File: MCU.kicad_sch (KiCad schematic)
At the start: 1 part, among them U2 STM32L476RGTx

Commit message: Partie écran
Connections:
- net EPD_RST: now reaches U2.15 (PA1)
- net EPD_DC: now reaches U2.16 (PA2)
- net EPD_BUSY: now reaches U2.17 (PA3)
- net EPD_CS: now reaches U2.20 (PA4)
- net EPD_SCK: now reaches U2.21 (PA5)
- net EPD_PWR: now reaches U2.22 (PA6)
- net EPD_DIN: now reaches U2.23 (PA7)
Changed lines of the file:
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@@
 	(wire
 		(pts
-			(xy 113.03 72.39) (xy 125.73 72.39)
+			(xy 114.3 128.27) (xy 125.73 128.27)
+		)
+		(stroke
+			(width 0)
+			(type default)
+		)
+	)
+	(wire
+		(pts
+			(xy 114.3 123.19) (xy 125.73 123.19)
+		)
+		(stroke
+			(width 0)
+			(type default)
+		)
+	)
+	(wire
+		(pts
+			(xy 114.3 72.39) (xy 125.73 72.39)
+		)
+		(stroke
+			(width 0)
+			(type default)
+		)
+	)
+	(wire
+		(pts
+			(xy 114.3 133.35) (xy 125.73 133.35)
 		)
 		(stroke
@@
 	(wire
 		(pts
-			(xy 113.03 69.85) (xy 125.73 69.85)
+			(xy 114.3 118.11) (xy 125.73 118.11)
+		)
+		(stroke
+			(width 0)
+			(type default)
+		)
+	)
+	(wire
+		(pts
+			(xy 114.3 130.81) (xy 125.73 130.81)
+		)
+		(stroke
+			(width 0)
+			(type default)
+		)
+	)
+	(wire
+		(pts
+			(xy 114.3 125.73) (xy 125.73 125.73)
+		)
+		(stroke
+			(width 0)
+			(type default)
+		)
+	)
+	(wire
+		(pts
+			(xy 114.3 69.85) (xy 125.73 69.85)
 		)
 		(stroke
@@
 		)
 	)
+	(wire
+		(pts
+			(xy 114.3 120.65) (xy 125.73 120.65)
+		)
+		(stroke
+			(width 0)
+			(type default)
+		)
+	)
+	(global_label "EPD_BUSY"
+		(shape input)
+		(at 114.3 128.27 180)
+		(fields_autoplaced yes)
+		(effects
+			(font
+				(size 1.27 1.27)
+			)
+			(justify right)
+		)
+		(property "Intersheetrefs" "${INTERSHEET_REFS}"
+			(at 101.7596 128.27 0)
+			(effects
+				(font
+					(size 1.27 1.27)
+				)
+				(justify right)
+				(hide yes)
+			)
+		)
+	)
+	(global_label "EPD_DC"
+		(shape input)
+		(at 114.3 130.81 180)
+		(fields_autoplaced yes)
+		(effects
+			(font
+				(size 1.27 1.27)
+			)
+			(justify right)
+		)
+		(property "Intersheetrefs" "${INTERSHEET_REFS}"
+			(at 104.1182 130.81 0)
+			(effects
+				(font
+					(size 1.27 1.27)
+				)
+				(justify right)
+				(hide yes)
+			)
+		)
+	)
+	(global_label "EPD_CS"
+		(shape input)
+		(at 114.3 125.73 180)
+		(fields_autoplaced yes)
+		(effects
+			(font
+				(size 1.27 1.27)
+			)
+			(justify right)
+		)
+		(property "Intersheetrefs" "${INTERSHEET_REFS}"
+			(at 104.1787 125.73 0)
+			(effects
+				(font
+					(size 1.27 1.27)
+				)
+				(justify right)
+				(hide yes)
+			)
+		)
+	)
 	(global_label "SCL"
 		(shape input)
-		(at 113.03 72.39 180)
-		(fields_autoplaced yes)
-		(effects
-			(font
-				(size 1.27 1.27)
-			)
-			(justify right)
-		)
-		(property "Intersheetrefs" "${INTERSHEET_REFS}"
-			(at 106.5372 72.39 0)
+		(at 114.3 72.39 180)
+		(fields_autoplaced yes)
+		(effects
+			(font
+				(size 1.27 1.27)
+			)
+			(justify right)
+		)
+		(property "Intersheetrefs" "${INTERSHEET_REFS}"
+			(at 107.8072 72.39 0)
+			(effects
+				(font
+					(size 1.27 1.27)
+				)
+				(justify right)
+				(hide yes)
+			)
+		)
+	)
+	(global_label "EPD_SCK"
+		(shape input)
+		(at 114.3 123.19 180)
+		(fields_autoplaced yes)
+		(effects
+			(font
+				(size 1.27 1.27)
+			)
+			(justify right)
+		)
+		(property "Intersheetrefs" "${INTERSHEET_REFS}"
+			(at 102.9087 123.19 0)
 			(effects
 				(font
@@
 	(global_label "SDA"
 		(shape input)
-		(at 113.03 69.85 180)
-		(fields_autoplaced yes)
-		(effects
-			(font
-				(size 1.27 1.27)
-			)
-			(justify right)
-		)
-		(property "Intersheetrefs" "${INTERSHEET_REFS}"
-			(at 106.4767 69.85 0)
-			(effects
-				(font
+		(at 114.3 69.85 180)
+		(fields_autoplaced yes)
+		(effects
+			(font
+				(size 1.27 1.27)
+			)
+			(justify right)
+		)
+		(property "Intersheetrefs" "${INTERSHEET_REFS}"
+			(at 107.7467 69.85 0)
+			(effects
+				(font
+					(size 1.27 1.27)
+				)
+				(justify right)
+				(hide yes)
+			)
+		)
+	)
+	(global_label "EPD_RST"
+		(shape input)
+		(at 114.3 133.35 180)
+		(fields_autoplaced yes)
+		(effects
+			(font
+				(size 1.27 1.27)
+			)
+			(justify right)
+		)
+		(property "Intersheetrefs" "${INTERSHEET_REFS}"
+			(at 103.2111 133.35 0)
+			(effects
+				(font
+					(size 1.27 1.27)
+				)
+				(justify right)
+				(hide yes)
+			)
+		)
+	)
+	(global_label "EPD_DIN"
+		(shape input)
+		(at 114.3 118.11 180)
+		(fields_autoplaced yes)
+		(effects
+			(font
+				(size 1.27 1.27)
+			)
+			(justify right)
+		)
+		(property "Intersheetrefs" "${INTERSHEET_REFS}"
+			(at 103.4529 118.11 0)
+			(effects
+				(font
+					(size 1.27 1.27)
+				)
+				(justify right)
+				(hide yes)
+			)
+		)
+	)
+	(global_label "EPD_PWR"
+		(shape input)
+		(at 114.3 120.65 180)
+		(fields_autoplaced yes)
+		(effects
+			(font
+				(size 1.27 1.27)
+			)
+			(justify right)
+		)
+		(property "Intersheetrefs" "${INTERSHEET_REFS}"
+			(at 102.6668 120.65 0)
+			(effects
+				(font

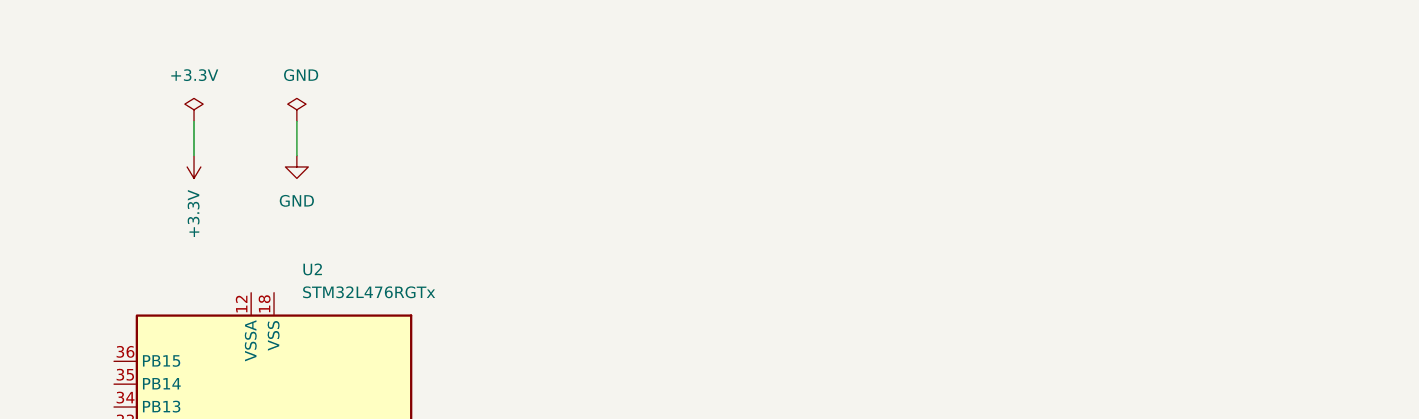
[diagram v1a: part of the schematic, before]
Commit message: Ajout total de la partie alimentation
Ajout de composant depuis un site internet ->OK
Fin de la partie écran et alimentation : ajout de tous les composants
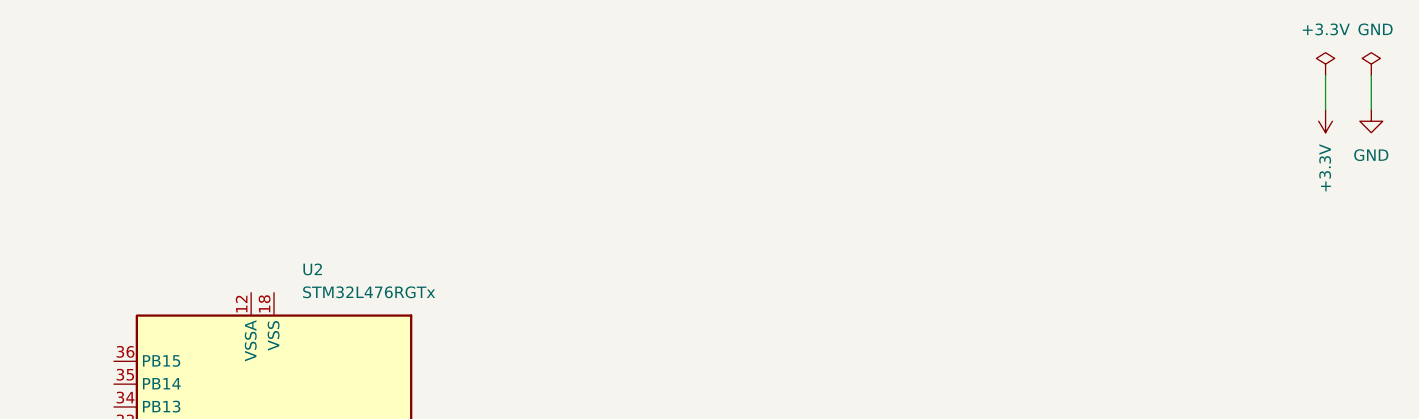
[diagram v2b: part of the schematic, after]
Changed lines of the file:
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@@
 	(wire
 		(pts
-			(xy 134.62 27.94) (xy 134.62 31.75)
+			(xy 260.35 22.86) (xy 260.35 26.67)
 		)
 		(stroke
@@
 	(wire
 		(pts
-			(xy 146.05 27.94) (xy 146.05 31.75)
+			(xy 265.43 22.86) (xy 265.43 26.67)
 		)
 		(stroke
@@
 	(symbol
 		(lib_id "power:PWR_FLAG")
-		(at 146.05 27.94 0)
+		(at 265.43 22.86 0)
 		(unit 1)
 		(exclude_from_sim no)
@@
 		(dnp no)
 		(property "Reference" "#FLG02"
-			(at 146.05 26.035 0)
+			(at 265.43 20.955 0)
 			(effects
 				(font
@@
 		)
 		(property "Value" "GND"
-			(at 144.526 22.86 0)
+			(at 263.906 17.78 0)
 			(effects
 				(font
@@
 		)
 		(property "Footprint" ""
-			(at 146.05 27.94 0)
+			(at 265.43 22.86 0)
 			(effects
 				(font
@@
 		)
 		(property "Datasheet" "~"
-			(at 146.05 27.94 0)
+			(at 265.43 22.86 0)
 			(effects
 				(font
@@
 		)
 		(property "Description" "Special symbol for telling ERC where power comes from"
-			(at 146.05 27.94 0)
+			(at 265.43 22.86 0)
 			(effects
 				(font
@@
 	(symbol
 		(lib_id "power:PWR_FLAG")
-		(at 134.62 27.94 0)
+		(at 260.35 22.86 0)
 		(unit 1)
 		(exclude_from_sim no)
@@
 		(fields_autoplaced yes)
 		(property "Reference" "#FLG01"
-			(at 134.62 26.035 0)
+			(at 260.35 20.955 0)
 			(effects
 				(font
@@
 		)
 		(property "Value" "+3.3V"
-			(at 134.62 22.86 0)
+			(at 260.35 17.78 0)
 			(effects
 				(font
@@
 		)
 		(property "Footprint" ""
-			(at 134.62 27.94 0)
+			(at 260.35 22.86 0)
 			(effects
 				(font
@@
 		)
 		(property "Datasheet" "~"
-			(at 134.62 27.94 0)
+			(at 260.35 22.86 0)
 			(effects
 				(font
@@
 		)
 		(property "Description" "Special symbol for telling ERC where power comes from"
-			(at 134.62 27.94 0)
+			(at 260.35 22.86 0)
 			(effects
 				(font
@@
 	(symbol
 		(lib_id "power:GND")
-		(at 146.05 31.75 0)
+		(at 265.43 26.67 0)
 		(unit 1)
 		(exclude_from_sim no)
@@
 		(fields_autoplaced yes)
 		(property "Reference" "#PWR05"
-			(at 146.05 38.1 0)
+			(at 265.43 33.02 0)
 			(effects
 				(font
@@
 		)
 		(property "Value" "GND"
-			(at 146.05 36.83 0)
+			(at 265.43 31.75 0)
 			(effects
 				(font
@@
 		)
 		(property "Footprint" ""
-			(at 146.05 31.75 0)
+			(at 265.43 26.67 0)
 			(effects
 				(font
@@
 		)
 		(property "Datasheet" ""
-			(at 146.05 31.75 0)
+			(at 265.43 26.67 0)
 			(effects
 				(font
@@
 		)
 		(property "Description" "Power symbol creates a global label with name \"GND\" , ground"
-			(at 146.05 31.75 0)
+			(at 265.43 26.67 0)
 			(effects
 				(font
@@
 	(symbol
 		(lib_id "power:+3.3V")
-		(at 134.62 31.75 180)
+		(at 260.35 26.67 180)
 		(unit 1)
 		(exclude_from_sim no)
@@
 		(dnp no)
 		(property "Reference" "#PWR04"
-			(at 134.62 27.94 0)
+			(at 260.35 22.86 0)
 			(effects
 				(font
@@
 		)
 		(property "Value" "+3.3V"
-			(at 134.6201 35.56 90)
+			(at 260.3501 30.48 90)
 			(effects
 				(font
@@
 		)
 		(property "Footprint" ""
-			(at 134.62 31.75 0)
+			(at 260.35 26.67 0)
 			(effects
 				(font
@@
 		)
 		(property "Datasheet" ""
-			(at 134.62 31.75 0)
+			(at 260.35 26.67 0)
 			(effects
 				(font
@@
 		)
 		(property "Description" "Power symbol creates a global label with name \"+3.3V\""
-			(at 134.62 31.75 0)
-			(effects
-				(font
+			(at 260.35 26.67 0)
+			(effects
+				(font

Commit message: Début Debug + MAJ MCU
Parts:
- added C19, C21, C22, C23: 100n, symbol Device:C_Small
- added C20: 4.7u, symbol Device:C_Small
- added C24: 1u, symbol Device:C_Small
- added C25: 10u, symbol Device:C_Small
- added C26, C27: 10p, symbol Device:C_Small
- added FB1: FerriteBead_Small, symbol Device:FerriteBead_Small
- added Y1: Crystal_GND24, symbol Device:Crystal_GND24
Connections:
- net GND: now also U2.12 (VSSA), U2.18 (VSS), U2.31 (VSS), U2.47 (VSS), U2.63 (VSS), C19.2, C20.2, C21.2, C22.2, C23.2, C24.2, C25.2, C26.1, C27.1, Y1.2 (G), Y1.4 (G)
- net at U2.1 (VBAT): now also U2.19 (VDD), U2.32 (VDD), U2.64 (VDD), C20.1, C21.1, C22.1, C23.1, FB1.1
- net at U2.13 (VDDA): now also C24.1, C25.1, FB1.2
- net at U2.3 (PC14): now also C27.2, Y1.1
- net at U2.4 (PC15): now also C26.2, Y1.3
- net SWDIO: now reaches U2.46 (PA13)
- net SWCLK: now reaches U2.49 (PA14)
- net JTDI: now reaches U2.50 (PA15)
- net TDO: now reaches U2.55 (PB3)
- net TRST: now reaches U2.56 (PB4)
- net nRST: now reaches U2.7 (NRST)
- net nRST: now also C19.1
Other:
- moved on the sheet: U2

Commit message: t
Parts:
- removed FB1: FerriteBead_Small, symbol Device:FerriteBead_Small
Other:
- note added: "Pad à mettre"
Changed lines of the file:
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@@
 	(generator_version "9.0")
 	(paper "A4")
-	(junction
-		(at 139.7 124.46)
-		(diameter 0)
-		(color 0 0 0 0)
+	(text "Pad à mettre"
+		(exclude_from_sim no)
+		(at 185.166 113.03 0)
+		(effects
+			(font
+				(size 1.27 1.27)
+			)
+		)
+	)
+	(text "Pad à mettre"
+		(exclude_from_sim no)
+		(at 168.148 107.95 0)
+		(effects
+			(font
+				(size 1.27 1.27)
+			)
+		)
 	)
 	(junction
@@
 	)
 	(junction
-		(at 123.19 124.46)
-		(diameter 0)
-		(color 0 0 0 0)
-	)
-	(junction
 		(at 186.69 59.69)
 		(diameter 0)
@@
 	(wire
 		(pts
-			(xy 134.62 124.46) (xy 139.7 124.46)
-		)
-		(stroke
-			(width 0)
-			(type default)
-		)
-	)
-	(wire
-		(pts
 			(xy 139.7 120.65) (xy 139.7 124.46)
 		)
@@
 		(pts
 			(xy 114.3 77.47) (xy 124.46 77.47)
-		)
-		(stroke
-			(width 0)
-			(type default)
-		)
-	)
-	(wire
-		(pts
-			(xy 123.19 124.46) (xy 129.54 124.46)
 		)
 		(stroke
@@
 					(unit 1)
 				)
-			)
-		)
-	)
-	(symbol
-		(lib_id "Device:FerriteBead_Small")
-		(at 132.08 124.46 270)
-		(unit 1)
-		(exclude_from_sim no)
-		(in_bom yes)
-		(on_board yes)
-		(dnp no)
-		(property "Reference" "FB1"
-			(at 131.826 128.016 90)
-			(effects
-				(font
-					(size 1.27 1.27)
-				)
-			)
-		)
-		(property "Value" "FerriteBead_Small"
-			(at 131.826 130.556 90)
-			(effects
-				(font
-					(size 1.27 1.27)
-				)
-			)
-		)
-		(property "Footprint" ""
-			(at 132.08 122.682 90)
-			(effects
-				(font
-					(size 1.27 1.27)
-				)
-				(hide yes)
-			)
-		)
-		(property "Datasheet" "~"
-			(at 132.08 124.46 0)
-			(effects
-				(font
-					(size 1.27 1.27)
-				)
-				(hide yes)
-			)
-		)
-		(property "Description" "Ferrite bead, small symbol"
-			(at 132.08 124.46 0)
-			(effects
-				(font
-					(size 1.27 1.27)
-				)
-				(hide yes)
-			)
-		)
-		(pin "2"
-		)
-		(pin "1"
-		)
-		(instances
-			(project ""
-				(path "/90bd0b60-6e70-43e1-8410-99fb54688c17/9ce3ae06-c5cc-4000-b6d8-5ae3d540ff9d"
-					(reference "FB1")
-					(unit 1)
-				)

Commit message: Dernieres pour review
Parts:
- added C28: 1u, symbol Device:C_Small
- added C5: 100n, symbol Device:C_Small
- added TP1: TestPoint, symbol Connector:TestPoint
- added TP2: TestPoint_Small, symbol Connector:TestPoint_Small
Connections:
- net +3.3V: now also C20.1, C21.1, C22.1, C23.1, C24.1, C25.1, U2.1 (VBAT), U2.13 (VDDA), U2.19 (VDD), U2.32 (VDD), U2.48 (VDDUSB), U2.64 (VDD), C28.1, C5.1
- net CMD_ALIM_SCREEN: now also U2.8 (PC0)
- net GND: now also C28.2, C5.2
- net nRST: now also TP2.1
- net TX: now reaches U2.42 (PA9)
- net RX: now reaches U2.43 (PA10)
- net at U2.60 (BOOT0): now also TP1.1
- net CMD_ALIM_BATTERY: now reaches U2.9 (PC1)
- net JTDI: no longer names the net of U2.50 (PA15)
- net TDO renamed SW0
- net TRST: no longer names the net of U2.56 (PB4)
- no-connect marks 0 -> 33
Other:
- note removed: "Pad à mettre"

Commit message: revue schema
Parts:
- added Y2: Crystal, symbol Device:Crystal
- C25: value 10u -> 10n
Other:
- note added: "+3 gpio/pad pour debug"
- note added: "ECX-.327-CDX-1293"
- note added: "J'ai cherché une ref de quartz précis, il a que 2 pin et il faut du 12.5pF"
- note added: "c'est quoi ce signal ?"
- note added: "faut bien connecté vddusb à vdd meme si on l'utilise pas, mais j'ai pas trouvé beaucoup d'info sur les capa bulk, de ce que je vois, une 100nF suffit"
- note added: "internal pull-up"
- note added: "mettre pull-down 10k"
- note added: "on a pas besoin d'uart vu qu'on a SWD"
- note added: "on peut en effet connecter vbat à vdd (ou le laisser en l'air) mais faut rajouter une 100nF"
- note added: "rajouter mesure_batterie sur une gpio adc_in"
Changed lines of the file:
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@@
 	(generator_version "9.0")
 	(paper "A4")
+	(text "ECX-.327-CDX-1293"
+		(exclude_from_sim no)
+		(at 247.65 42.418 0)
+		(effects
+			(font
+				(size 1.27 1.27)
+			)
+		)
+	)
+	(text "c'est quoi ce signal ?"
+		(exclude_from_sim no)
+		(at 93.98 62.23 0)
+		(effects
+			(font
+				(size 1.27 1.27)
+				(color 255 9 0 1)
+			)
+		)
+	)
+	(text "+3 gpio/pad pour debug"
+		(exclude_from_sim no)
+		(at 109.728 33.02 0)
+		(effects
+			(font
+				(size 1.27 1.27)
+				(color 255 9 0 1)
+			)
+		)
+	)
+	(text "rajouter mesure_batterie sur une gpio adc_in"
+		(exclude_from_sim no)
+		(at 186.69 71.12 0)
+		(effects
+			(font
+				(size 1.27 1.27)
+				(color 255 0 0 1)
+			)
+		)
+	)
+	(text "on peut en effet connecter vbat à vdd (ou le laisser en l'air) mais faut rajouter une 100nF"
+		(exclude_from_sim no)
+		(at 187.452 140.208 0)
+		(effects
+			(font
+				(size 1.27 1.27)
+				(color 255 9 0 1)
+			)
+		)
+	)
+	(text "on a pas besoin d'uart vu qu'on a SWD"
+		(exclude_from_sim no)
+		(at 87.122 89.154 0)
+		(effects
+			(font
+				(size 1.27 1.27)
+				(color 255 9 0 1)
+			)
+		)
+	)
+	(text "J'ai cherché une ref de quartz précis, \nil a que 2 pin et il faut du 12.5pF"
+		(exclude_from_sim no)
+		(at 233.934 60.96 0)
+		(effects
+			(font
+				(size 1.27 1.27)
+				(color 255 9 0 1)
+			)
+		)
+	)
+	(text "internal pull-up"
+		(exclude_from_sim no)
+		(at 186.69 113.538 0)
+		(effects
+			(font
+				(size 1.27 1.27)
+			)
+		)
+	)
+	(text "mettre pull-down 10k"
+		(exclude_from_sim no)
+		(at 199.136 107.95 0)
+		(effects
+			(font
+				(size 1.27 1.27)
+				(color 255 9 0 1)
+			)
+		)
+	)
+	(text "faut bien connecté vddusb à vdd meme si on l'utilise pas, \nmais j'ai pas trouvé beaucoup d'info sur les capa bulk, \nde ce que je vois, une 100nF suffit"
+		(exclude_from_sim no)
+		(at 65.786 141.478 0)
+		(effects
+			(font
+				(size 1.27 1.27)
+				(color 255 9 0 1)
+			)
+		)
+	)
 	(junction
 		(at 209.55 53.34)
@@
 	)
 	(symbol
+		(lib_id "Device:Crystal")
+		(at 224.79 41.91 90)
+		(unit 1)
+		(exclude_from_sim no)
+		(in_bom yes)
+		(on_board yes)
+		(dnp no)
+		(fields_autoplaced yes)
+		(property "Reference" "Y2"
+			(at 228.6 40.6399 90)
+			(effects
+				(font
+					(size 1.27 1.27)
+				)
+				(justify right)
+			)
+		)
+		(property "Value" "Crystal"
+			(at 228.6 43.1799 90)
+			(effects
+				(font
+					(size 1.27 1.27)
+				)
+				(justify right)
+			)
+		)
+		(property "Footprint" ""
+			(at 224.79 41.91 0)
+			(effects
+				(font
+					(size 1.27 1.27)
+				)
+				(hide yes)
+			)
+		)
+		(property "Datasheet" "~"
+			(at 224.79 41.91 0)
+			(effects
+				(font
+					(size 1.27 1.27)
+				)
+				(hide yes)
+			)
+		)
+		(property "Description" "Two pin crystal"
+			(at 224.79 41.91 0)
+			(effects
+				(font
+					(size 1.27 1.27)
+				)
+				(hide yes)
+			)
+		)
+		(pin "2"
+		)
+		(pin "1"
+		)
+		(instances
+			(project ""
+				(path "/90bd0b60-6e70-43e1-8410-99fb54688c17/9ce3ae06-c5cc-4000-b6d8-5ae3d540ff9d"
+					(reference "Y2")
+					(unit 1)
+				)
+			)
+		)
+	)
+	(symbol
 		(lib_id "Device:C_Small")
 		(at 105.41 127 0)
@@
 			)
 		)
-		(property "Value" "10u"
+		(property "Value" "10n"
 			(at 107.95 130.048 0)
 			(effects

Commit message: premieres modif depuis la review
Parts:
- removed Y1: Crystal_GND24, symbol Device:Crystal_GND24
- added C30: 100n, symbol Device:C_Small
- added R5: 10k, symbol Device:R
- C26, C27: value 10p -> 12.5p
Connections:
- net +3.3V: now also C30.1
- net GND: now also C30.2, R5.1
- net at C27.2, U2.3 (PC14): now also Y2.1
- net at C26.2, U2.4 (PC15): now also Y2.2
- net MEASURE_BATTERY: now reaches U2.11 (PC3)
- net at TP1.1, U2.60 (BOOT0): now also R5.2
- net RX: no longer names the net of U2.43 (PA10)
- net SW0: no longer names the net of U2.55 (PB3)
- net TX: no longer names the net of U2.42 (PA9)
- no-connect marks 33 -> 35
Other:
- note removed: "J'ai cherché une ref de quartz précis, il a que 2 pin et il faut du 12.5pF"
- note removed: "c'est quoi ce signal ?"
- note removed: "mettre pull-down 10k"
- note removed: "on a pas besoin d'uart vu qu'on a SWD"
- note removed: "rajouter mesure_batterie sur une gpio adc_in"
- moved on the sheet: Y2

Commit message: t
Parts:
- added TP3, TP4, TP5: TestPoint, symbol Connector:TestPoint
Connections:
- net DEBUG2: now reaches U2.26 (PB0)
- net DEBUG2: now also TP4.1
- net DEBUG1: now reaches U2.36 (PB15)
- net DEBUG1: now also TP3.1
- net DEBUG3: now reaches U2.38 (PC7)
- net DEBUG3: now also TP5.1
- no-connect marks 35 -> 32
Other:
- note removed: "+3 gpio/pad pour debug"
- note removed: "faut bien connecté vddusb à vdd meme si on l'utilise pas, mais j'ai pas trouvé beaucoup d'info sur les capa bulk, de ce que je vois, une 100nF suffit"
- note removed: "on peut en effet connecter vbat à vdd (ou le laisser en l'air) mais faut rajouter une 100nF"
